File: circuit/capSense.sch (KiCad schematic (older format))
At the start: 16 parts, among them P1 Capsense, P2 PWR_IN, P3 RS 232 TTL, P4 gpio, SW1 SW_PUSH, U1 ESP-12E

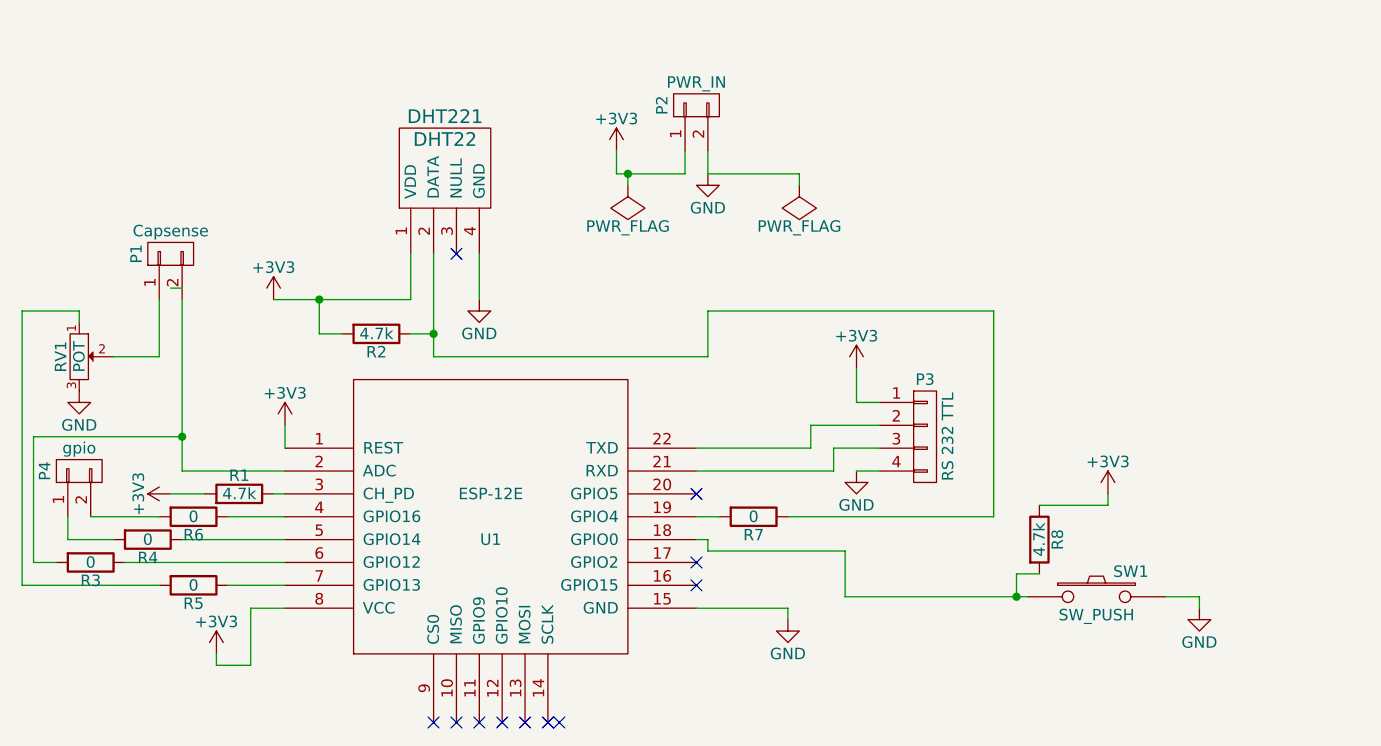
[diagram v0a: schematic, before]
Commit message: new version of PCB with support for waterlog
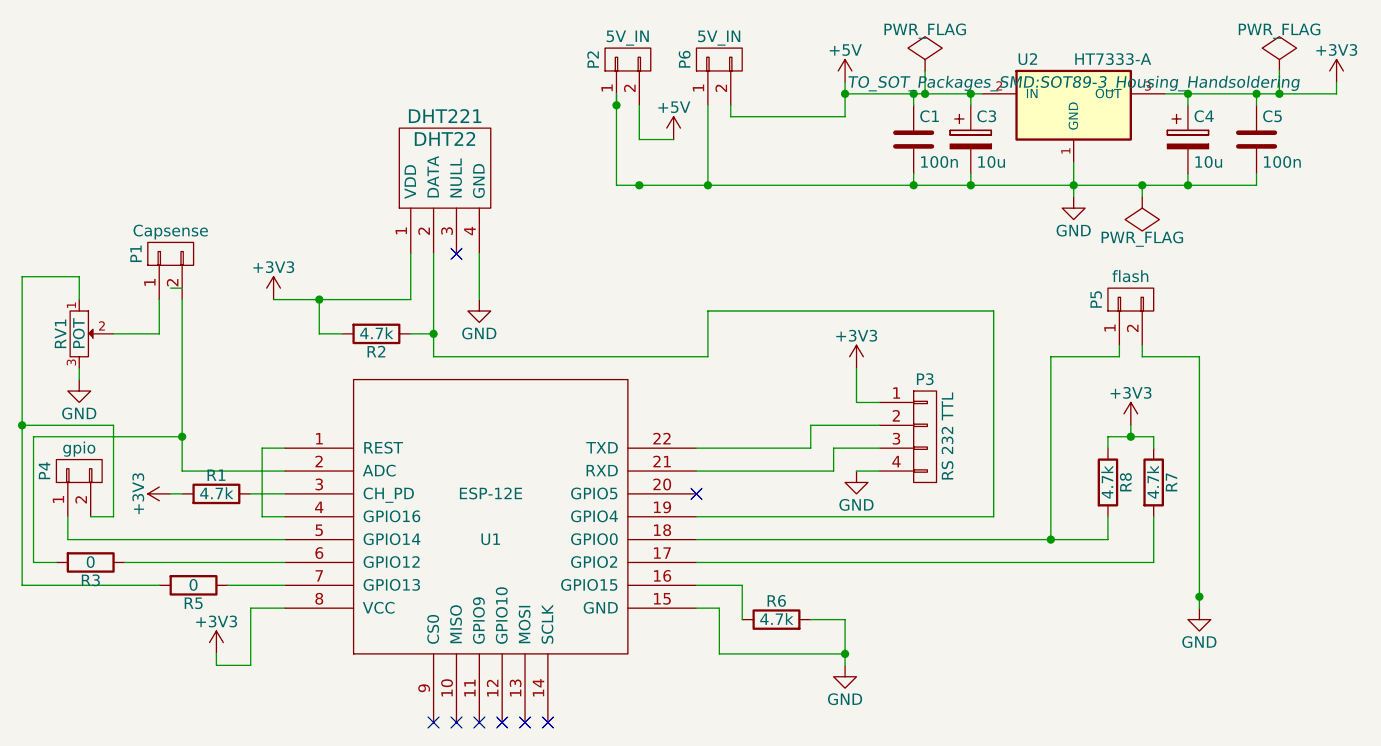
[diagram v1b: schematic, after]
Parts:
- removed R4: 0, Resistors_SMD:R_0603, symbol R
- removed SW1: SW_PUSH, Buttons_Switches_SMD:SW_SPST_PTS645, symbol SW_PUSH
- added C1, C5: 100n, Capacitors_SMD:C_0805_HandSoldering, symbol C
- added C3, C4: 10u, Capacitors_Tantalum_SMD:TantalC_SizeC_EIA-6032_HandSoldering, symbol CP
- added P5: flash, Socket_Strips:Socket_Strip_Straight_1x02, symbol CONN_01X02
- added P6: 5V_IN, Socket_Strips:Socket_Strip_Straight_1x02, symbol CONN_01X02
- added U2: HT7333-A, TO_SOT_Packages_SMD:SOT89-3_Housing_Handsoldering, symbol HT7333-A
- P2: value PWR_IN -> 5V_IN
- R1, R2, R3, R5, R8: footprint Resistors_SMD:R_0603 -> Resistors_SMD:R_0805_HandSoldering
- R6, R7: value 0 -> 4.7k; footprint Resistors_SMD:R_0603 -> Resistors_SMD:R_0805_HandSoldering
- RV1: footprint Potentiometers:Potentiometer_Trimmer-Piher-PT15-h2-5_vertical -> Potentiometers:Potentiometer_Bourns_3296Z_3-8Zoll_Angular_ScrewFront
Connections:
- net labels added: +5V
- wire segments 68 -> 94
- no-connect marks 11 -> 8
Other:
- moved on the sheet: R1, R8, RV1
